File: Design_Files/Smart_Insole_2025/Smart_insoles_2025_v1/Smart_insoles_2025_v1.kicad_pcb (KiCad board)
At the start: 4 copper layers, 69.7 x 32.1 mm, 9 parts, among them J1 Conn_01x20, U1 ESP32-C3_SUPERMINI_SMD, U2 CD74HC4067M96

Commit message: updated Schematic & PCB layout
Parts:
- added C2: C, Capacitor_SMD:C_0603_1608Metric_Pad1.08x0.95mm_HandSolder, F.Cu at (95.8, 30.7)
- added C3: C, Capacitor_SMD:C_0603_1608Metric_Pad1.08x0.95mm_HandSolder, F.Cu at (119.9, 27.2)
- added J2: Conn_01x02_Pin, Connector_JST:JST_EH_S2B-EH_1x02_P2.50mm_Horizontal, B.Cu at (134.0, 23.0)
- RN1, RN2: value R_Pack04 -> 10k
- moved BT1 29.5 mm to (110.7, 6.96)
- moved RN2 2.02 mm to (104.0, 28.5), turned to -90 degrees
- moved RN1 1.56 mm to (112.3, 28.6), turned to -90 degrees
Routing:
- net /INT: track 0.00 -> 59.7 mm, vias 0 -> 2
- net VCC: track 24.6 -> 78.6 mm, vias 0 -> 10
- net /SDA: track 0.00 -> 48.9 mm, vias 0 -> 2
- net /SCL: track 0.00 -> 48.2 mm, vias 0 -> 2
- net /SIG: track 0.00 -> 25.8 mm, vias 0 -> 2
- net /I1: track 0.00 -> 13.1 mm
- net /I3: track 0.00 -> 12.5 mm
- net /I0: track 0.00 -> 12.2 mm
- net /I6: track 0.00 -> 11.8 mm
- net /I7: track 0.00 -> 11.4 mm
- net /I2: track 0.00 -> 11.3 mm
- net /I5: track 0.00 -> 11.2 mm
- net /I4: track 0.00 -> 11.1 mm
- net GND: track 28.8 -> 30.9 mm, vias 14 -> 16

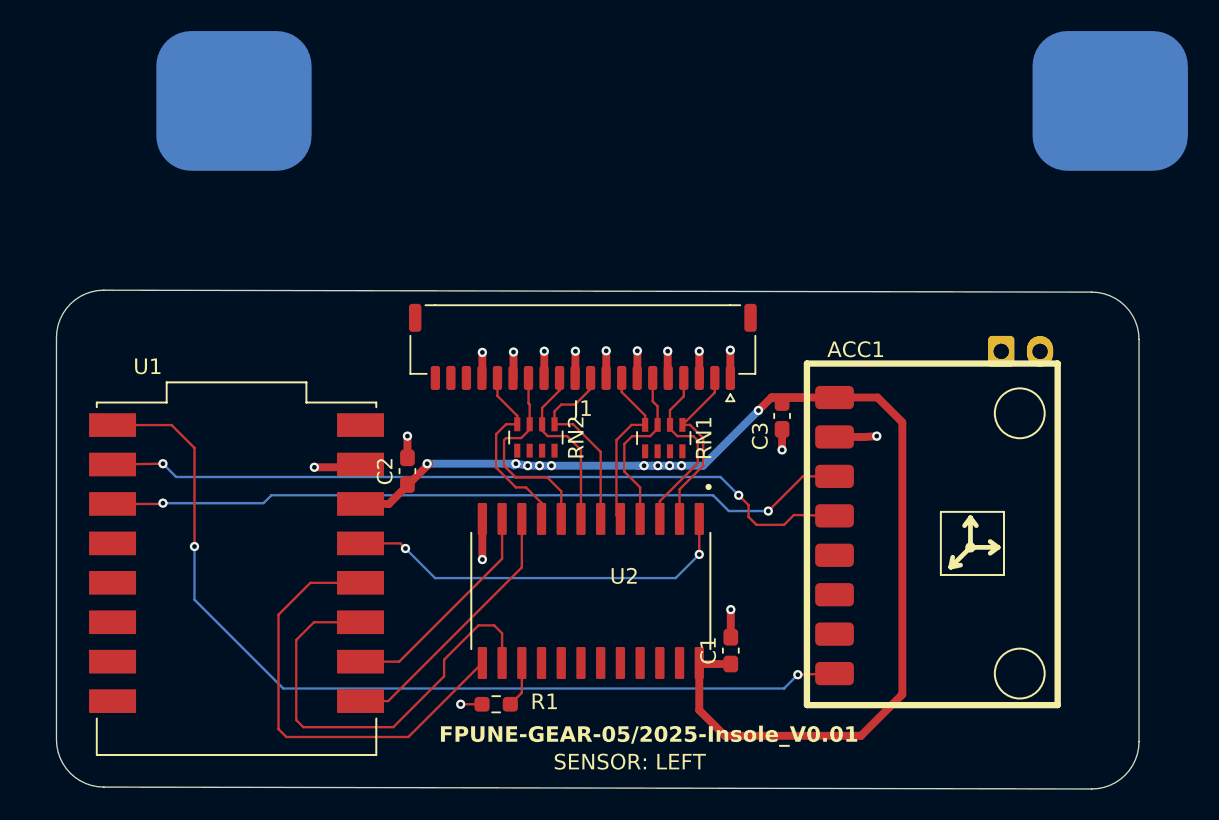
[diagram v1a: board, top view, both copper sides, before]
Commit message: Changing MCU orientation + Rerouting
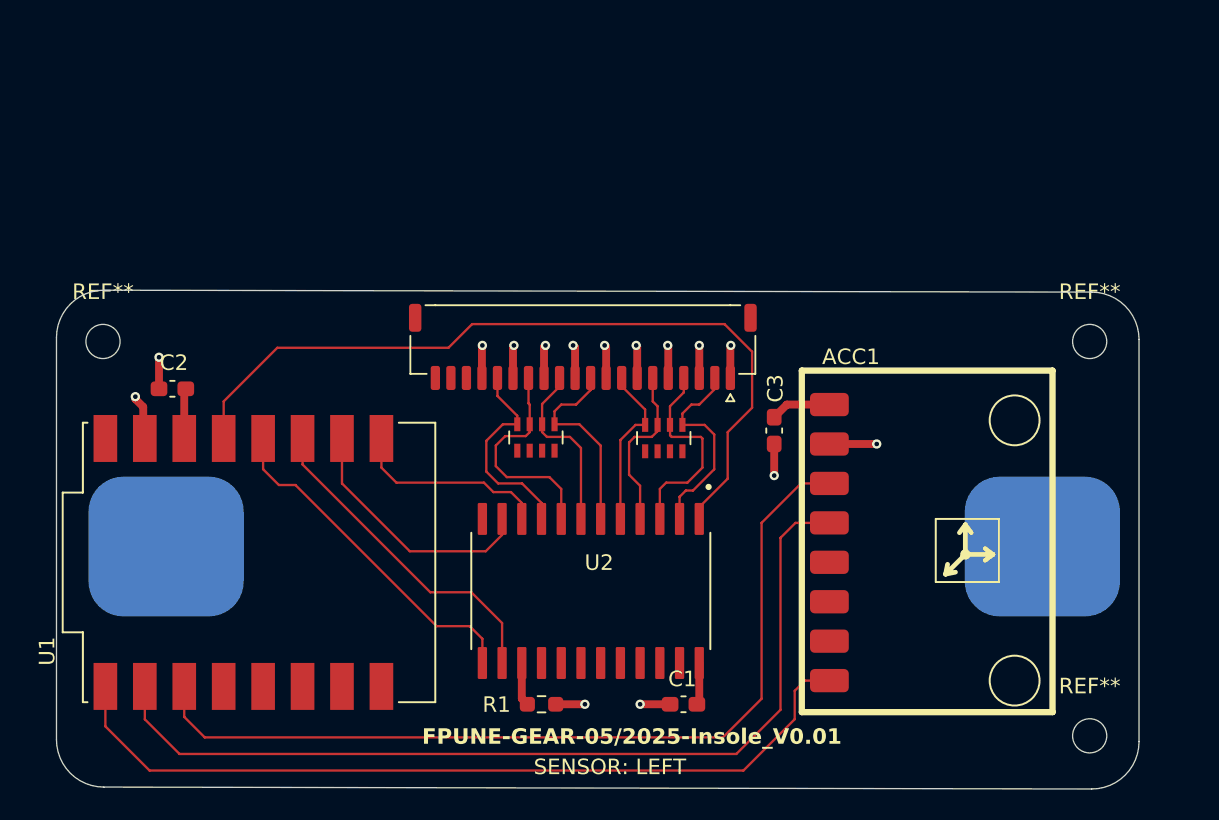
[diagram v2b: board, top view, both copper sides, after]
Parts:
- removed J2: Conn_01x02_Pin, Connector_JST:JST_EH_S2B-EH_1x02_P2.50mm_Horizontal
- added REF**: MountingHole_2.2mm_M2, MountingHole:MountingHole_2.2mm_M2, F.Cu at (139.7, 22.4)
- added REF**: MountingHole_2.2mm_M2, MountingHole:MountingHole_2.2mm_M2, F.Cu at (76.1, 22.4)
- added REF**: MountingHole_2.2mm_M2, MountingHole:MountingHole_2.2mm_M2, F.Cu at (139.7, 47.8)
- moved BT1 28.5 mm to (110.5, 35.5), turned to -90 degrees
- moved C2 16.0 mm to (80.6, 25.4), turned to 180 degrees
- moved C1 4.61 mm to (113.5, 45.7), turned to 180 degrees
- moved R1 2.92 mm to (104.4, 45.7), turned to 0 degrees
- moved U1 1.79 mm to (86.2, 36.6), turned to 90 degrees
- moved C3 1.07 mm to (119.4, 28.1)
- moved ACC1 0.56 mm to (121.2, 46.2)
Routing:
- net VCC: track 78.6 -> 9.86 mm, vias 10 -> 0
- net /SIG: track 25.8 -> 51.4 mm, vias 2 -> 0
- net /SDA: track 48.9 -> 59.8 mm, vias 2 -> 0
- net /SCL: track 48.2 -> 57.5 mm, vias 2 -> 0
- net /S2: track 28.7 -> 21.3 mm
- net /S3: track 28.8 -> 22.2 mm
- net /INT: track 59.7 -> 53.9 mm, vias 2 -> 0
- net /S0: track 17.1 -> 12.9 mm
- net GND: track 30.9 -> 33.6 mm, vias 16 -> 15
- net /S1: track 14.4 -> 16.5 mm
- net /I7: track 11.4 -> 13.1 mm
- net /I6: track 11.8 -> 13.4 mm
- net /I0: track 12.2 -> 13.4 mm
- net /I1: track 13.1 -> 14.1 mm

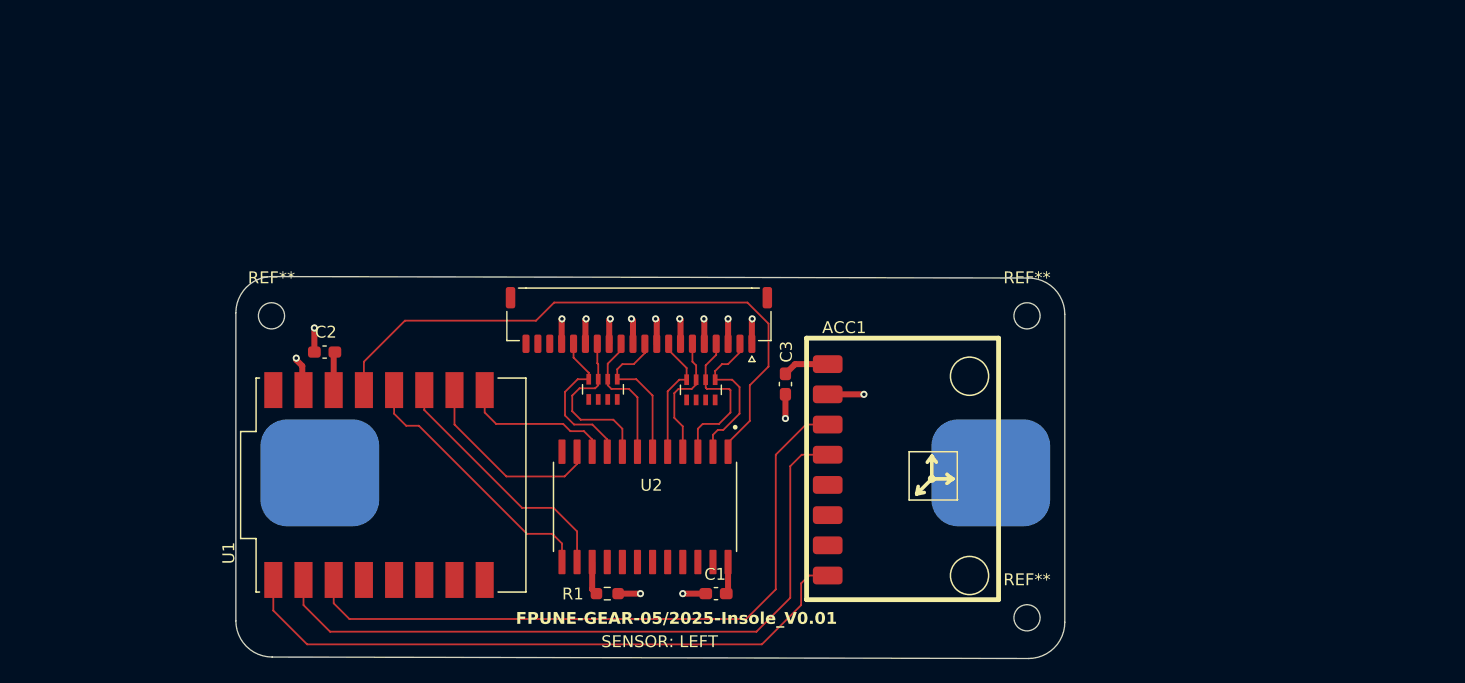
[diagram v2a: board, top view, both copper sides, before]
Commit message: modified project outline and routing.
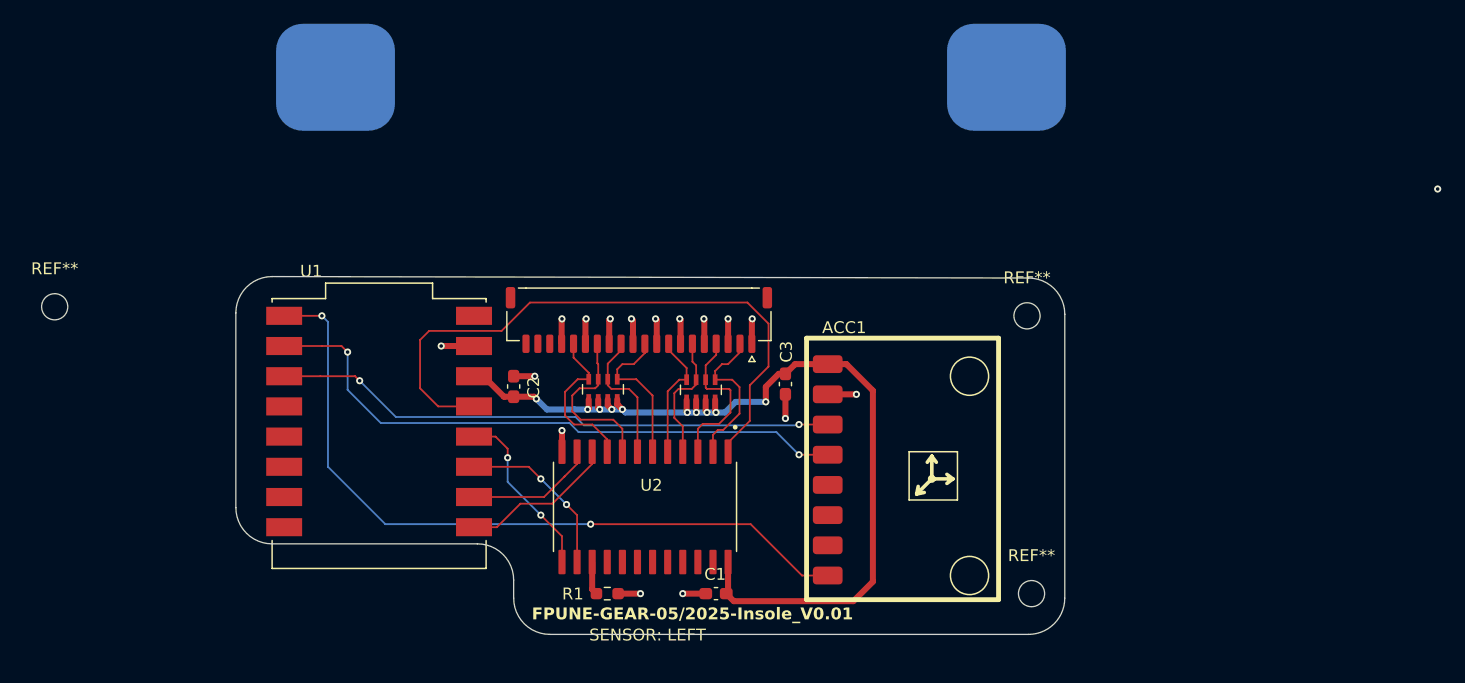
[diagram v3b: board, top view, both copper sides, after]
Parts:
- moved BT1 33.3 mm to (111.8, 2.18)
- moved REF** 18.3 mm to (57.9, 21.6)
- moved C2 16.2 mm to (96.5, 28.3), turned to 90 degrees
- moved U1 4.45 mm to (85.2, 32.3), turned to 0 degrees
- moved REF** 2.07 mm to (140.1, 45.7)
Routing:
- net VCC: track 9.86 -> 78.3 mm, vias 0 -> 10
- net /SCL: track 57.5 -> 47.5 mm, vias 0 -> 2
- net /SDA: track 59.8 -> 51.4 mm, vias 0 -> 2
- net /INT: track 53.9 -> 61.9 mm, vias 0 -> 2
- net /S3: track 22.2 -> 14.7 mm, vias 0 -> 2
- net /S2: track 21.3 -> 14.3 mm, vias 0 -> 2
- net /S1: track 16.5 -> 10.9 mm
- net /SIG: track 51.4 -> 52.8 mm
- net GND: track 33.6 -> 33.7 mm, vias 15 -> 16
- net (no net): vias 0 -> 1
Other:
- board size 69.7 x 32.1 mm -> 69.7 x 30.1 mm

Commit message: Change accelerometer to Lsm6ds033
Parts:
- removed ACC1: GY-521, GY-521:GY-521_SMD
- removed BT1: Battery_Cell, BAT_LIFEPO4:Lifepo4_3.2v_300mAh_holder
- removed REF** (x3): MountingHole_2.2mm_M2, MountingHole:MountingHole_2.2mm_M2
- removed RN2: 10k, Resistor_SMD:R_Array_Concave_4x0603
- added C10: 10nF, Capacitor_SMD:C_0603_1608Metric_Pad1.08x0.95mm_HandSolder, F.Cu at (30.5, 49.5)
- added C11: 10nF, Capacitor_SMD:C_0603_1608Metric_Pad1.08x0.95mm_HandSolder, F.Cu at (30.5, 52.0)
- added C12: 10nF, Capacitor_SMD:C_0603_1608Metric_Pad1.08x0.95mm_HandSolder, F.Cu at (34.8, 34.5)
- added C13: 10nF, Capacitor_SMD:C_0603_1608Metric_Pad1.08x0.95mm_HandSolder, F.Cu at (34.8, 37.0)
- added C14: 100nF, Capacitor_SMD:C_0603_1608Metric_Pad1.08x0.95mm_HandSolder, F.Cu at (56.9, 39.0)
- added C15: 100nF, Capacitor_SMD:C_0603_1608Metric_Pad1.08x0.95mm_HandSolder, F.Cu at (56.9, 41.5)
- added C17: 1uF, Capacitor_SMD:C_0603_1608Metric_Pad1.08x0.95mm_HandSolder, F.Cu at (34.8, 39.5)
- added C18: 1uF, Capacitor_SMD:C_0603_1608Metric_Pad1.08x0.95mm_HandSolder, F.Cu at (34.8, 42.0)
- added C4: 1uF, Capacitor_SMD:C_0603_1608Metric_Pad1.08x0.95mm_HandSolder, F.Cu at (30.5, 34.5)
- added C5: 1uF, Capacitor_SMD:C_0603_1608Metric_Pad1.08x0.95mm_HandSolder, F.Cu at (30.5, 37.0)
- added C6: 10nF, Capacitor_SMD:C_0603_1608Metric_Pad1.08x0.95mm_HandSolder, F.Cu at (30.5, 39.5)
- added C7: 10nF, Capacitor_SMD:C_0603_1608Metric_Pad1.08x0.95mm_HandSolder, F.Cu at (30.5, 42.0)
- added C8: 10nF, Capacitor_SMD:C_0603_1608Metric_Pad1.08x0.95mm_HandSolder, F.Cu at (30.5, 44.5)
- added C9: 10nF, Capacitor_SMD:C_0603_1608Metric_Pad1.08x0.95mm_HandSolder, F.Cu at (30.5, 47.0)
- added J2: Conn_01x02_Pin, Connector_JST:JST_EH_S2B-EH_1x02_P2.50mm_Horizontal, F.Cu at (58.3, 33.1)
- added R10: 100k, Resistor_SMD:R_0603_1608Metric_Pad0.98x0.95mm_HandSolder, F.Cu at (39.2, 34.5)
- added R11: 100k, Resistor_SMD:R_0603_1608Metric_Pad0.98x0.95mm_HandSolder, F.Cu at (39.2, 37.0)
- added R14: 100k, Resistor_SMD:R_0603_1608Metric_Pad0.98x0.95mm_HandSolder, F.Cu at (39.2, 39.5)
- added R15: 100k, Resistor_SMD:R_0603_1608Metric_Pad0.98x0.95mm_HandSolder, F.Cu at (39.2, 42.0)
- added R18: 3.5k, Resistor_SMD:R_0603_1608Metric_Pad0.98x0.95mm_HandSolder, F.Cu at (39.2, 44.5)
- added R3: 100k, Resistor_SMD:R_0603_1608Metric_Pad0.98x0.95mm_HandSolder, F.Cu at (34.8, 44.5)
- added R4: 100k, Resistor_SMD:R_0603_1608Metric_Pad0.98x0.95mm_HandSolder, F.Cu at (34.8, 47.0)
- added R6: 100k, Resistor_SMD:R_0603_1608Metric_Pad0.98x0.95mm_HandSolder, F.Cu at (34.8, 49.5)
- added R8: 100k, Resistor_SMD:R_0603_1608Metric_Pad0.98x0.95mm_HandSolder, F.Cu at (34.8, 52.0)
- added U4: ~, ADM8829:SOT95P280X145-6N, F.Cu at (51.1, 46.6)
- added U8: MCP6004-I_ST, MCP6004_I_ST:SOP65P640X120-14N, F.Cu at (56.2, 57.9)
- C1, C2, C3: value C -> 1uF
- moved RN1 50.5 mm to (63.3, 41.0), turned to 0 degrees
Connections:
- J1 pad 10: /I3 -> unconnected-(J1-Pin_10-Pad10)
- J1 pad 12: /I2 -> unconnected-(J1-Pin_12-Pad12)
- J1 pad 14: /I1 -> unconnected-(J1-Pin_14-Pad14)
- J1 pad 16: /I0 -> unconnected-(J1-Pin_16-Pad16)
- J1 pad 2: /I7 -> unconnected-(J1-Pin_2-Pad2)
- J1 pad 4: /I6 -> unconnected-(J1-Pin_4-Pad4)
- J1 pad 6: /I5 -> unconnected-(J1-Pin_6-Pad6)
- J1 pad 8: /I4 -> unconnected-(J1-Pin_8-Pad8)
- RN1 pad 1: /I7 -> /CS
- RN1 pad 2: /I6 -> /SDO/SA0
- RN1 pad 3: /I5 -> /SDA
- RN1 pad 4: /I4 -> /SCL

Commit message: Added battery connector footprint. Grouping componnets in PcbNew
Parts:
- removed J2: Conn_01x02_Pin, Connector_JST:JST_EH_S2B-EH_1x02_P2.50mm_Horizontal
- added J3: S2B-PH-SM4-TB_LF__SN_, JST-PH2-2.00MM-SMD-HORIZONTAL:JST_S2B-PH-SM4-TB_LF__SN_, F.Cu at (55.2, 26.5)
- added R12: TC33X-2-302E, 3x3_TrimPot:TRIM_TC33X-2-302E, F.Cu at (55.5, 66.1)
- added R16: TC33X-2-302E, 3x3_TrimPot:TRIM_TC33X-2-302E, F.Cu at (47.4, 66.3)
- added R17: TC33X-2-302E, 3x3_TrimPot:TRIM_TC33X-2-302E, F.Cu at (54.1, 54.0)
- added R19: TC33X-2-302E, 3x3_TrimPot:TRIM_TC33X-2-302E, F.Cu at (47.9, 53.9)
- added R2: TC33X-2-302E, 3x3_TrimPot:TRIM_TC33X-2-302E, F.Cu at (85.2, 64.0)
- added R5: TC33X-2-302E, 3x3_TrimPot:TRIM_TC33X-2-302E, F.Cu at (85.2, 57.7)
- added R7: TC33X-2-302E, 3x3_TrimPot:TRIM_TC33X-2-302E, F.Cu at (69.4, 57.6)
- added R9: TC33X-2-302E, 3x3_TrimPot:TRIM_TC33X-2-302E, F.Cu at (69.8, 63.8)
- added U3: LSM6DSO32TR, LDM6S032TR:XDCR_LSM6DSO32TR, F.Cu at (133.8, 31.9)
- added U9: MCP6004-I_ST, MCP6004_I_ST:SOP65P640X120-14N, F.Cu at (51.8, 59.1)
- moved C14 78.6 mm to (135.5, 36.0), turned to -90 degrees
- moved C15 75.9 mm to (132.7, 36.1), turned to -90 degrees
- moved RN1 71.8 mm to (133.8, 27.6), turned to 90 degrees
- moved C7 63.5 mm to (90.0, 64.3), turned to 90 degrees
- moved C8 61.9 mm to (91.0, 57.4), turned to -90 degrees
- moved R4 51.3 mm to (84.4, 60.4), turned to 180 degrees
- moved R3 51.3 mm to (83.3, 61.4), turned to 180 degrees
- moved C6 46.1 mm to (73.2, 56.8), turned to 90 degrees
- moved C9 38.7 mm to (65.2, 64.0), turned to -90 degrees
- moved R8 38.0 mm to (71.6, 61.5)
- moved R6 38.0 mm to (71.2, 60.4)
- moved C13 36.7 mm to (59.7, 63.9), turned to 90 degrees
- moved C12 31.1 mm to (59.0, 54.0), turned to 90 degrees
- moved C17 30.4 mm to (58.0, 59.1)
- moved R11 28.6 mm to (51.7, 62.7)
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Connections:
- C12 pad 2: /I4 -> /I5
- C7 pad 1: unconnected-(C7-Pad1) -> /FSR_AnalogFE/FSR_OUT_0
- C7 pad 2: unconnected-(C7-Pad2) -> /I0

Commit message: PCBNew. AFE component grouping
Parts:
- J3: moved to B.Cu
- moved J3 82.3 mm to (135.8, 43.3), turned to 90 degrees
- moved C8 36.0 mm to (64.1, 33.4), turned to 90 degrees
- moved R5 34.8 mm to (60.2, 33.4), turned to 180 degrees
- moved C7 33.0 mm to (64.1, 43.9)
- moved R2 32.2 mm to (60.1, 43.9), turned to 180 degrees
- moved R4 31.5 mm to (62.5, 37.7)
- moved R6 30.6 mm to (50.5, 37.8)
- moved R8 30.5 mm to (50.6, 39.3)
- moved R3 30.3 mm to (62.6, 39.2)
- moved R7 30.3 mm to (51.2, 33.4)
- moved U8 29.7 mm to (56.7, 38.6)
- moved C6 29.4 mm to (55.3, 33.4)
- moved R9 27.3 mm to (51.1, 43.9), turned to 180 degrees
- moved R16 26.8 mm to (32.8, 43.9)
- moved R12 26.6 mm to (40.9, 43.9)
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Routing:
- net /I1: track 14.1 -> 0.00 mm
- net /I6: track 13.4 -> 0.00 mm
- net /I0: track 13.4 -> 0.00 mm
- net /I7: track 13.1 -> 0.00 mm
- net /I3: track 12.8 -> 0.00 mm
- net /I2: track 11.4 -> 0.00 mm
- net /I5: track 10.9 -> 0.00 mm
- net /I4: track 10.7 -> 0.00 mm
- net /SIG: track 52.8 -> 44.2 mm
- net VCC: track 78.3 -> 72.0 mm, vias 10 -> 2
- net unconnected-(J1-Pin_10-Pad10): track 0.00 -> 4.50 mm
- net unconnected-(J1-Pin_2-Pad2): track 0.00 -> 4.18 mm
- net unconnected-(J1-Pin_8-Pad8): track 0.00 -> 3.65 mm
- net unconnected-(J1-Pin_12-Pad12): track 0.00 -> 3.45 mm
- net unconnected-(J1-Pin_4-Pad4): track 0.00 -> 3.39 mm
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
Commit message: PCBnew:Moving placed components. Fixed REF of mcp component
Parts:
- added C16: 1uF, Capacitor_SMD:C_0603_1608Metric, F.Cu at (149.8, 32.2)
- added C19: 1uF, Capacitor_SMD:C_0603_1608Metric, F.Cu at (149.8, 34.8)
- added D1: LED, LED_SMD:LED_0603_1608Metric, F.Cu at (153.9, 32.3)
- added D2: LED, LED_SMD:LED_0603_1608Metric, F.Cu at (153.9, 34.9)
- added R13: 540, Resistor_SMD:R_0603_1608Metric, F.Cu at (149.8, 37.3)
- added R20: 1.5k, Resistor_SMD:R_0603_1608Metric, F.Cu at (149.8, 39.8)
- added R21: 1.5k, Resistor_SMD:R_0603_1608Metric, F.Cu at (149.8, 42.3)
- U8, U9: footprint MCP6004_I_ST:SOP65P640X120-14N -> MCP6004_I_ST:custom
- moved R18 83.0 mm to (112.3, 46.5)
- moved C18 82.5 mm to (113.9, 46.5)
- moved R16 81.9 mm to (114.7, 41.0)
- moved C11 81.8 mm to (118.2, 41.1)
- moved U4 81.4 mm to (117.0, 46.5)
- moved C4 81.2 mm to (117.1, 44.0)
- moved R7 81.0 mm to (132.1, 30.5)
- moved C10 81.0 mm to (117.3, 30.7)
- moved R19 81.0 mm to (113.7, 30.7)
- moved U9 80.8 mm to (119.1, 35.7)
- moved C17 80.7 mm to (125.2, 35.6)
- moved R10 80.7 mm to (125.2, 33.8)
- moved R11 80.7 mm to (125.2, 37.3)
- moved R12 80.7 mm to (121.6, 40.9)
- moved R14 80.7 mm to (112.8, 35.1)
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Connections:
- J1 pad 10: unconnected-(J1-Pin_10-Pad10) -> /I3
- J1 pad 12: unconnected-(J1-Pin_12-Pad12) -> /I2
- J1 pad 14: unconnected-(J1-Pin_14-Pad14) -> /I1
- J1 pad 16: unconnected-(J1-Pin_16-Pad16) -> /I0
- J1 pad 2: unconnected-(J1-Pin_2-Pad2) -> /I7
- J1 pad 4: unconnected-(J1-Pin_4-Pad4) -> /I6
- J1 pad 6: unconnected-(J1-Pin_6-Pad6) -> /I5
- J1 pad 8: unconnected-(J1-Pin_8-Pad8) -> /I4
- J3 pad 2: -BATT -> GND
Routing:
- net VCC: track 72.0 -> 0.00 mm, vias 2 -> 0
- net /INT: track 61.9 -> 0.00 mm, vias 2 -> 0
- net /SDA: track 51.4 -> 0.00 mm, vias 2 -> 0
- net /SCL: track 47.5 -> 0.00 mm, vias 2 -> 0
- net /SIG: track 44.2 -> 0.00 mm
- net GND: track 34.3 -> 0.00 mm, vias 16 -> 0
- net /S2: track 15.4 -> 0.00 mm, vias 2 -> 0
- net /S3: track 15.3 -> 0.00 mm, vias 2 -> 0
- net /S0: track 12.9 -> 0.00 mm
- net /S1: track 10.3 -> 0.00 mm
- net Net-(U2-~{E}): track 4.60 -> 0.00 mm
- net unconnected-(J1-Pin_10-Pad10): track 4.50 -> 0.00 mm
- net unconnected-(J1-Pin_2-Pad2): track 4.18 -> 0.00 mm
- net unconnected-(J1-Pin_8-Pad8): track 3.65 -> 0.00 mm
- net unconnected-(J1-Pin_12-Pad12): track 3.45 -> 0.00 mm
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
